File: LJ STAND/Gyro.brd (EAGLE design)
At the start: 30.5 x 20.3 mm, 20 parts

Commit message: Main edits, light gate pcbs
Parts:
- C11, C3, C7: value 0.1uF -> 1uF
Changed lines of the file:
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@@
 <?xml version="1.0" encoding="utf-8"?>
 <!DOCTYPE eagle SYSTEM "eagle.dtd">
-<eagle version="8.6.3">
+<eagle version="8.7.0">
 <drawing>
 <settings>
@@
 <attribute name="VALUE" x="7.112" y="10.033" size="0.4064" layer="28" font="vector" rot="MR0"/>
 </element>
-<element name="C3" library="SparkFun-Capacitors" package="0603-CAP" value="0.1uF" x="23.622" y="13.462" smashed="yes" rot="MR0">
+<element name="C3" library="SparkFun-Capacitors" package="0603-CAP" value="1uF" x="23.622" y="13.462" smashed="yes" rot="MR0">
 <attribute name="VALUE" x="24.638" y="12.319" size="0.4064" layer="28" font="vector" rot="MR0"/>
 </element>
@@
 <attribute name="VALUE" x="16.002" y="7.747" size="0.4064" layer="28" font="vector" rot="MR0"/>
 </element>
-<element name="C7" library="SparkFun-Capacitors" package="0603-CAP" value="0.1uF" x="23.622" y="11.176" smashed="yes" rot="MR0">
+<element name="C7" library="SparkFun-Capacitors" package="0603-CAP" value="1uF" x="23.622" y="11.176" smashed="yes" rot="MR0">
 <attribute name="VALUE" x="24.638" y="10.033" size="0.4064" layer="28" font="vector" rot="MR0"/>
 </element>
@@
 <attribute name="VALUE" x="7.112" y="12.319" size="0.4064" layer="28" font="vector" rot="MR0"/>
 </element>
-<element name="C11" library="SparkFun-Capacitors" package="0603-CAP" value="0.1uF" x="14.986" y="13.462" smashed="yes" rot="MR0">
+<element name="C11" library="SparkFun-Capacitors" package="0603-CAP" value="1uF" x="14.986" y="13.462" smashed="yes" rot="MR0">
 <attribute name="VALUE" x="16.002" y="12.319" size="0.4064" layer="28" font="vector" rot="MR0"/>
 </element>

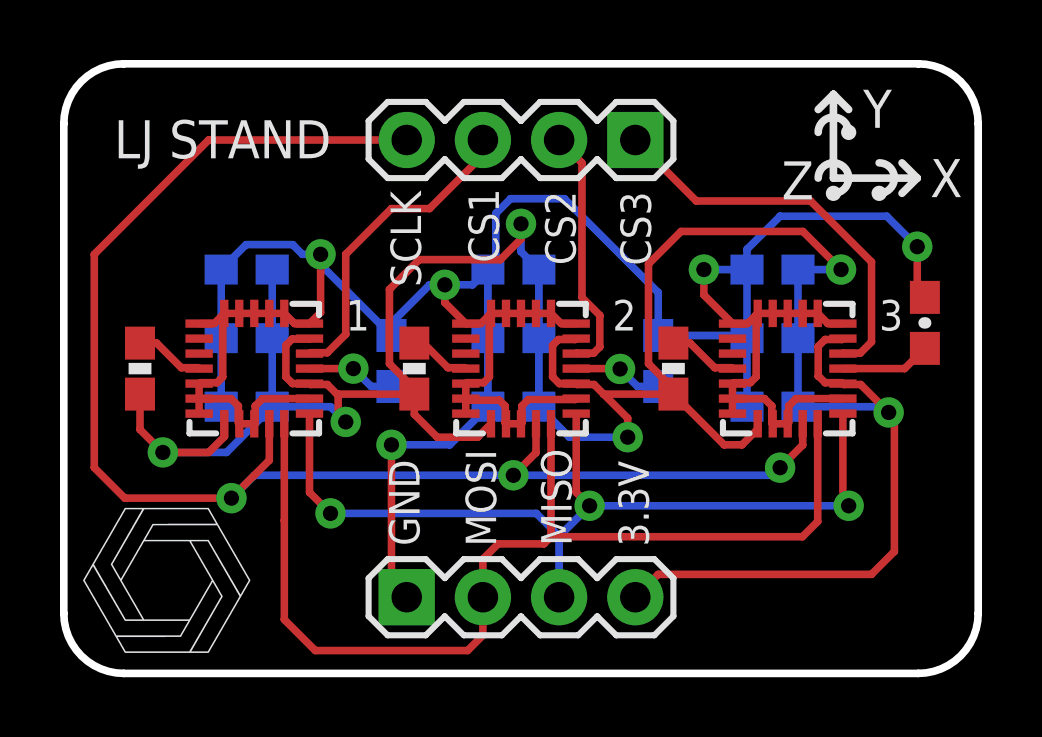
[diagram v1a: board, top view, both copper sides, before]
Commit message: Finalisation of gyro, encoder and light boards + gerbers, silkscreen fixes
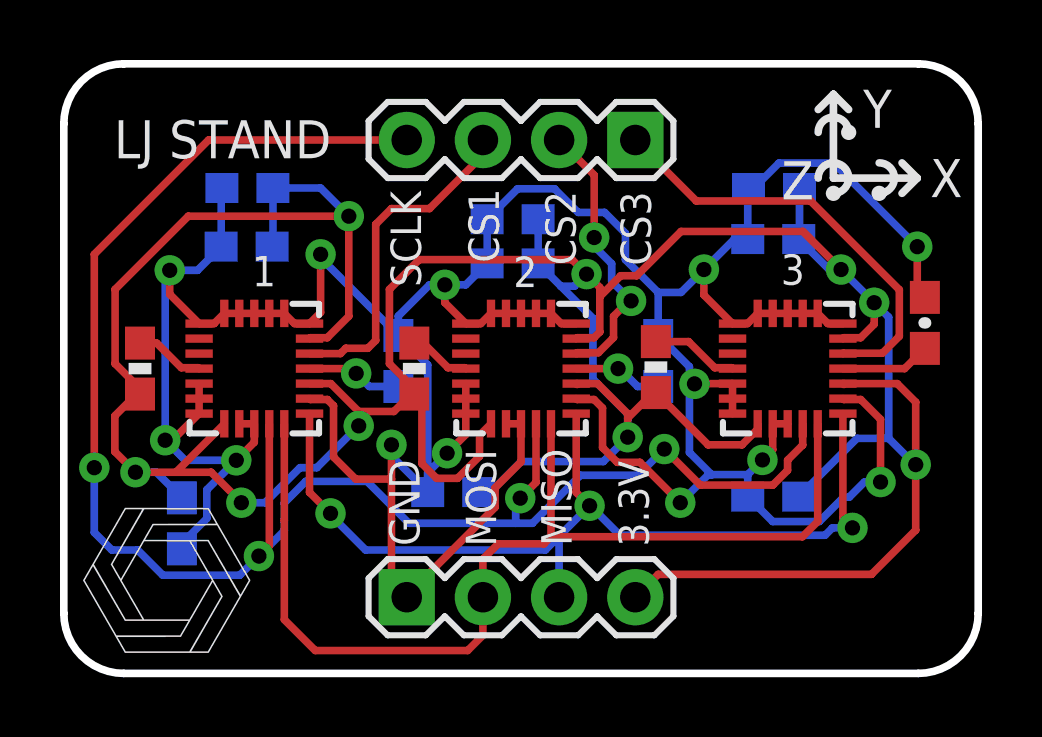
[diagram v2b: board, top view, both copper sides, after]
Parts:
- moved C1 4.45 mm to (3.94, 5.00), turned to 270 degrees
- moved C6 3.48 mm to (13.0, 6.05)
- moved C7 3.30 mm to (23.6, 14.5)
- moved C2 3.05 mm to (6.10, 14.2)
- moved C5 3.00 mm to (23.6, 5.89)
- moved C3 2.72 mm to (23.7, 16.2)
- moved C10 2.72 mm to (6.12, 16.2)
- moved C9 2.49 mm to (15.0, 13.7)
- moved C11 1.68 mm to (15.0, 15.1)
- moved R3 0.59 mm to (19.7, 10.2)
- moved C4 0.23 mm to (11.2, 10.4)
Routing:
- net 3.3V: track 98.6 -> 131.2 mm, vias 6 -> 9
- net GND: track 103.7 -> 133.3 mm, vias 5 -> 13
- net SCLK: track 49.6 -> 59.0 mm, vias 3 -> 4
- net MISO: track 30.1 -> 31.9 mm
- net CS3: track 13.3 -> 14.5 mm
- net CS2: track 8.34 -> 9.35 mm, vias 0 -> 2
- net CS1: track 10.6 -> 11.3 mm
- net N$4: track 2.32 -> 2.93 mm
